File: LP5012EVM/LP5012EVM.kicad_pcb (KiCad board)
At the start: 2 copper layers, 16.2 x 24.5 mm, 14 parts, among them J1 Main Connector, U1 LP5012

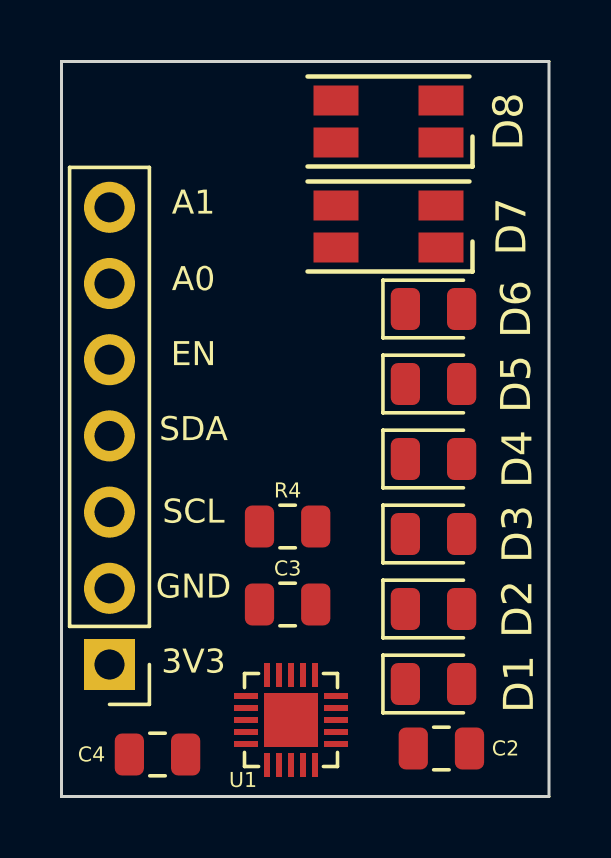
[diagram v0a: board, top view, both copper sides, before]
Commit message: Avance de ruteo
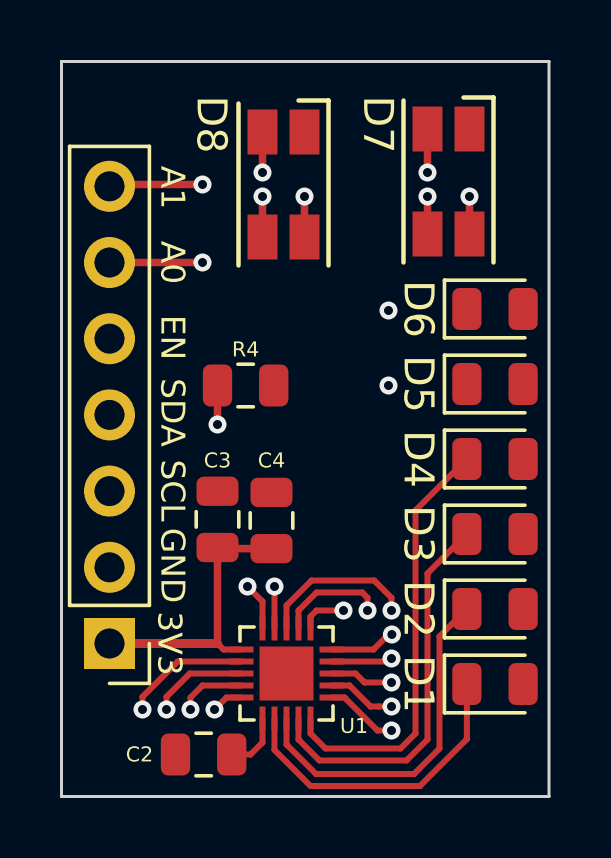
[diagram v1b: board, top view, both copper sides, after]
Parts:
- moved C4 8.68 mm to (147.1, 90.8), turned to 90 degrees
- moved C2 7.93 mm to (144.8, 98.6), turned to 180 degrees
- moved R4 4.90 mm to (146.2, 86.3)
- moved D8 4.08 mm to (147.5, 79.6), turned to 270 degrees
- moved C3 3.68 mm to (145.3, 90.8), turned to 90 degrees
- moved D7 2.50 mm to (153.0, 79.5), turned to 270 degrees
- moved D1 2.05 mm to (154.6, 96.2)
- moved D2 2.05 mm to (154.6, 93.8)
- moved D3 2.05 mm to (154.6, 91.2)
- moved D4 2.05 mm to (154.6, 88.8)
- moved D5 2.05 mm to (154.6, 86.2)
- moved D6 2.05 mm to (154.6, 83.8)
- moved U1 1.56 mm to (147.6, 95.9)
- moved J1 0.70 mm to (141.7, 94.9)
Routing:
- net /LB3: track 0.00 -> 14.3 mm
- net /LB2: track 0.00 -> 13.0 mm
- net /LB1: track 0.00 -> 11.8 mm
- net /LB0: track 0.00 -> 10.4 mm
- net VCC: track 0.00 -> 9.50 mm
- net /LB11: track 0.00 -> 6.62 mm, vias 0 -> 2
- net /LB10: track 0.00 -> 5.00 mm, vias 0 -> 2
- net /ADDR1: track 0.00 -> 4.73 mm, vias 0 -> 2
- net /ADDR0: track 0.00 -> 4.50 mm, vias 0 -> 2
- net /SDA: track 0.00 -> 4.21 mm, vias 0 -> 1
- net /LB8: track 0.00 -> 3.67 mm, vias 0 -> 2
- net /LB6: track 0.00 -> 3.37 mm, vias 0 -> 2
- net /LB7: track 0.00 -> 3.29 mm, vias 0 -> 2
- net /SCL: track 0.00 -> 3.25 mm, vias 0 -> 1
- net /LB9: track 0.00 -> 2.93 mm, vias 0 -> 2
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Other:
- outline, holes or cut-outs redrawn

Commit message: Inclusión de avance de PCB
Inclusión de planos, queda pendiente agregar modelos 3D de agunos componentes
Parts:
- moved D8 0.10 mm to (147.5, 79.5)
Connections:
- J1 pad 6: /ADDR0 -> /ADDR1
- J1 pad 7: /ADDR1 -> /ADDR0
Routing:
- net /LB6: track 3.37 -> 27.3 mm
- net /LB7: track 3.29 -> 23.4 mm
- net /LB8: track 3.67 -> 22.8 mm
- net /LB5: track 2.29 -> 20.2 mm
- net /LB11: track 6.62 -> 24.0 mm
- net /LB4: track 2.46 -> 18.7 mm
- net /LB9: track 2.93 -> 17.9 mm
- net /LB10: track 5.00 -> 19.7 mm
- net /IN_EN: track 2.27 -> 16.2 mm
- net /ADDR0: track 4.50 -> 17.1 mm, vias 2 -> 1
- net Net-(R4-Pad1): track 2.37 -> 12.7 mm
- net VCC: track 9.50 -> 19.6 mm, vias 0 -> 3
- net /ADDR1: track 4.73 -> 14.3 mm, vias 2 -> 1
- net /SDA: track 4.21 -> 10.4 mm
- net /SCL: track 3.25 -> 8.61 mm
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- added copper zone on B.Cu, net GND
- added copper zone on F.Cu, net GND
- added copper zone on B.Cu, net VCC
- added copper zone on F.Cu, net VCC

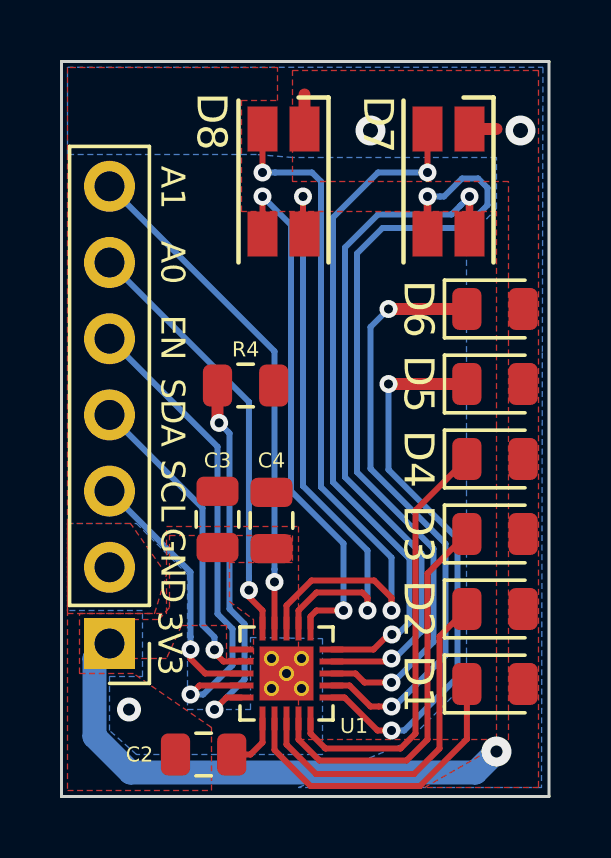
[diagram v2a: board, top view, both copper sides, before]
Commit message: Corrección de DRCs
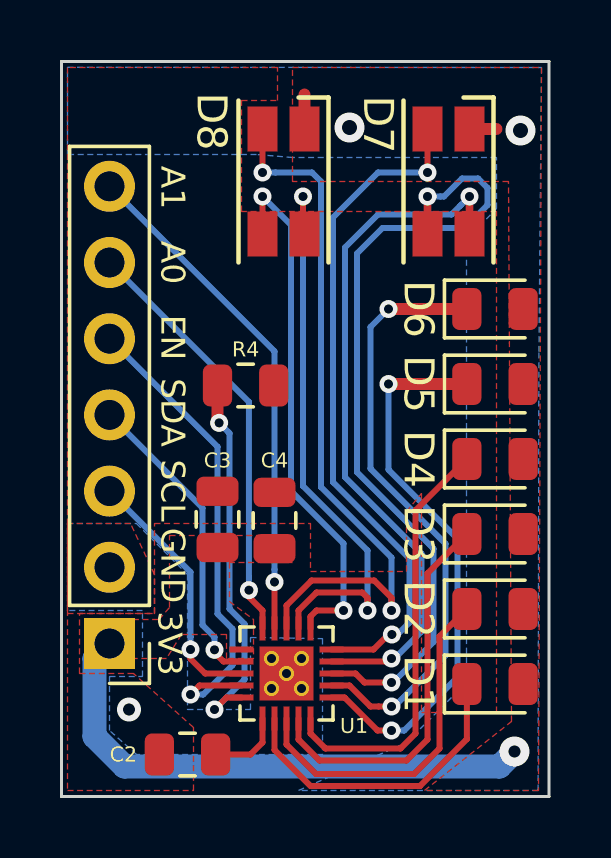
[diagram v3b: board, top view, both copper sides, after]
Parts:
- moved C2 0.54 mm to (144.3, 98.6)
- moved C4 0.10 mm to (147.2, 90.8)
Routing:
- net Net-(C2-Pad1): track 1.99 -> 2.53 mm
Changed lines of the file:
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@@
   (page A4)
   (layers
-    (0 F.Cu signal hide)
+    (0 F.Cu signal)
     (31 B.Cu signal)
     (32 B.Adhes user hide)
@@
     (35 F.Paste user hide)
     (36 B.SilkS user hide)
-    (37 F.SilkS user hide)
+    (37 F.SilkS user)
     (38 B.Mask user hide)
     (39 F.Mask user hide)
@@
   )
   (setup
-    (last_trace_width 0.8)
+    (last_trace_width 0.25)
     (user_trace_width 0.2)
     (user_trace_width 0.4)
@@
   )
   (module Capacitor_SMD:C_0805_2012Metric (layer F.Cu)
-    (at 144.8375 98.6 180)
+    (at 144.3 98.6 180)
     (descr "Capacitor SMD 0805 (2012 Metric), square (rectangular) end terminal, IPC_7351 nominal, (Body size source: https://docs.google.com/spreadsheets/d/1BsfQQcO9C6DZCsRaXUlFlo91Tg2WpOkGARC1WS5S8t0/edit?usp=sharing), generated with kicad-footprint-generator")
     (tags capacitor)
@@
   )
   (module Capacitor_SMD:C_0805_2012Metric (layer F.Cu)
-    (at 147.1 90.8 90)
+    (at 147.2 90.8 90)
     (descr "Capacitor SMD 0805 (2012 Metric), square (rectangular) end terminal, IPC_7351 nominal, (Body size source: https://docs.google.com/spreadsheets/d/1BsfQQcO9C6DZCsRaXUlFlo91Tg2WpOkGARC1WS5S8t0/edit?usp=sharing), generated with kicad-footprint-generator")
     (tags capacitor)
@@
   (gr_line (start 140.1 100) (end 140.1 75.5) (layer Edge.Cuts) (width 0.1))
   (gr_line (start 140.1 75.5) (end 156.35 75.5) (layer Edge.Cuts) (width 0.1))
-  (via (at 154.6 98.5) (size 1) (drill 0.4) (layers F.Cu B.Cu) (net 3) (status 1000000))
-  (segment (start 142.4 99.2) (end 153.9 99.2) (width 0.8) (layer B.Cu) (net 3) (status 1000000))
-  (segment (start 153.9 99.2) (end 154.6 98.5) (width 0.8) (layer B.Cu) (net 3) (status 1000000))
-  (segment (start 141.2 95.4) (end 141.2 98) (width 0.8) (layer B.Cu) (net 3) (status 1000000))
-  (segment (start 141.7 94.9) (end 141.2 95.4) (width 0.8) (layer B.Cu) (net 3) (status 1000000))
-  (segment (start 141.2 98) (end 142.4 99.2) (width 0.8) (layer B.Cu) (net 3) (status 1000000))
-  (segment (start 146.4 98.6) (end 145.775 98.6) (width 0.2) (layer F.Cu) (net 1))
+  (segment (start 146.4 98.6) (end 145.2375 98.6) (width 0.2) (layer F.Cu) (net 1))
   (segment (start 146.8 97.4) (end 146.8 98.2) (width 0.2) (layer F.Cu) (net 1))
   (segment (start 146.8 98.2) (end 146.4 98.6) (width 0.2) (layer F.Cu) (net 1))
@@
   (segment (start 148.2 77.75) (end 148.2 76.6) (width 0.4) (layer F.Cu) (net 3))
   (segment (start 153.7 77.75) (end 154.6 77.75) (width 0.4) (layer F.Cu) (net 3))
-  (via (at 150.4 77.8) (size 1) (drill 0.5) (layers F.Cu B.Cu) (net 3))
+  (via (at 149.7 77.7) (size 1) (drill 0.5) (layers F.Cu B.Cu) (net 3))
   (via (at 155.4 77.8) (size 1) (drill 0.5) (layers F.Cu B.Cu) (net 3))
+  (via (at 155.199998 98.5) (size 1) (drill 0.4) (layers F.Cu B.Cu) (net 3))
+  (segment (start 141.7 94.9) (end 141.2 95.4) (width 0.8) (layer B.Cu) (net 3))
+  (segment (start 141.2 95.4) (end 141.2 98) (width 0.8) (layer B.Cu) (net 3))
+  (segment (start 141.2 98) (end 142.199999 98.999999) (width 0.8) (layer B.Cu) (net 3))
+  (segment (start 154.699999 98.999999) (end 155.199998 98.5) (width 0.8) (layer B.Cu) (net 3))
+  (segment (start 142.199999 98.999999) (end 154.699999 98.999999) (width 0.8) (layer B.Cu) (net 3))
   (segment (start 153.6125 98.0875) (end 153.6125 96.25) (width 0.2) (layer F.Cu) (net 4))
   (segment (start 152.05001 99.64999) (end 153.6125 98.0875) (width 0.2) (layer F.Cu) (net 4))
@@
     (polygon
       (pts
-        (xy 156 99.7) (xy 152.2 99.7) (xy 155 98.1) (xy 155 79.5) (xy 147.8 79.5)
-        (xy 147.8 75.8) (xy 156 75.8)
+        (xy 156 99.8) (xy 152.2 99.8) (xy 155.1 97.5) (xy 155 79.5) (xy 147.8 79.5)
+        (xy 147.8 75.7) (xy 156.1 75.7)
       )
     )
@@
         (xy 141.2 94.1) (xy 143.35 94.1) (xy 143.7 93.7) (xy 143.7 91.3) (xy 147.8 91.3)
         (xy 147.8 92.2) (xy 145.7 92.2) (xy 145.7 93.5) (xy 146.5 94.1) (xy 146.5 95.4)
-        (xy 145.6 95.4) (xy 145.6 94.3) (xy 144.1 94.3) (xy 143.6 95.4) (xy 141.2 95.4)
+        (xy 145.6 95.4) (xy 145.6 94.6) (xy 144.1 94.6) (xy 143.6 95.4) (xy 141.2 95.4)
       )
     )
@@
     (polygon
       (pts
-        (xy 145.1 99.8) (xy 145.1 97.7) (xy 142.5 95.9) (xy 140.7 95.9) (xy 140.7 93.9)
-        (xy 143.6 93.9) (xy 143.6 92.6) (xy 142.4 90.9) (xy 140.3 90.9) (xy 140.3 99.8)
+        (xy 144.5 99.8) (xy 144.5 97.7) (xy 142.5 95.9) (xy 140.7 95.9) (xy 140.7 93.9)
+        (xy 143.2 93.9) (xy 143.2 92.6) (xy 142.4 90.9) (xy 140.3 90.9) (xy 140.3 99.8)
       )
     )
@@
   (zone (net 2) (net_name GND) (layer F.Cu) (hatch edge 0.508)
     (connect_pads (clearance 0.1))
-    (min_thickness 0.0254)
-    (fill yes (arc_segments 32) (thermal_gap 0.4) (thermal_bridge_width 0.8) (smoothing fillet) (radius 1))
+    (min_thickness 0.1)
+    (fill yes (arc_segments 32) (thermal_gap 0.4) (thermal_bridge_width 0.8) (smoothing fillet) (radius 0.5))
     (polygon
       (pts
-        (xy 143.2 93.9) (xy 143.6 92.6) (xy 143.6 91) (xy 148 91) (xy 148 98.1)
-        (xy 154.6 98.1) (xy 154.6 87.7) (xy 154.6 80.5) (xy 146.1 80.5) (xy 146.1 76.8)
-        (xy 147.3 76.8) (xy 147.3 75.7) (xy 140.3 75.7) (xy 140.3 93.9)
+        (xy 143.2 93.9) (xy 143.2 92.6) (xy 143.2 90.9) (xy 148.4 90.9) (xy 148.4 92.5)
+        (xy 151.6 92.5) (xy 151.6 90.5) (xy 152.1 89.9) (xy 152.1 97.2) (xy 154.6 97.2)
+        (xy 154.6 87.7) (xy 154.6 80.5) (xy 146.1 80.5) (xy 146.1 76.8) (xy 147.3 76.8)
+        (xy 147.3 75.7) (xy 140.3 75.7) (xy 140.3 93.9)
       )
     )
@@
     (polygon
       (pts
-        (xy 156.128385 85.203608) (xy 156.1 99.7) (xy 148 99.7) (xy 151.6 98.2) (xy 153.6 96.2)
+        (xy 156.014193 85.201804) (xy 155.985808 99.798196) (xy 148 99.8) (xy 151.6 98.2) (xy 153.6 96.2)
         (xy 153.6 90.95) (xy 153.6 81.45) (xy 154.6 80.4) (xy 154.6 78.7) (xy 147.8 78.7)
-        (xy 146.6 78.6) (xy 140.3 78.6) (xy 140.3 75.69286) (xy 156.14824 75.69286)
+        (xy 146.6 78.6) (xy 140.3 78.6) (xy 140.3 75.69286) (xy 156.1 75.7)
       )
     )

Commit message: Inclusión de algunos aspectos de la corrección del compañero
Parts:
- added FD1: Fiducial_0.5mm_Mask1mm, Fiducial:Fiducial_0.5mm_Mask1mm, F.Cu at (141.7, 76.8)
- added G***: LOGO, Footprint Logo:Logo_Smartium, B.Cu at (153.7, 89.1)
- U1: footprint Footprint LP5012:PQFN21P40_300X300X80L40X20T180 -> Footprint LP5012:LP5012
- renumbered C3 to CE
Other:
- board text added: "Designed In Argentina Made In China"
- board text added: "Led Driver Version 1.0"
